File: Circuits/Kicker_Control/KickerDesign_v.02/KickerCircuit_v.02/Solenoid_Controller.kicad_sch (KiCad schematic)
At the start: 8 parts, among them Q2 NMOS, U3 VS-5EWH06FN-M3, U4 VS-5EWH06FN-M3

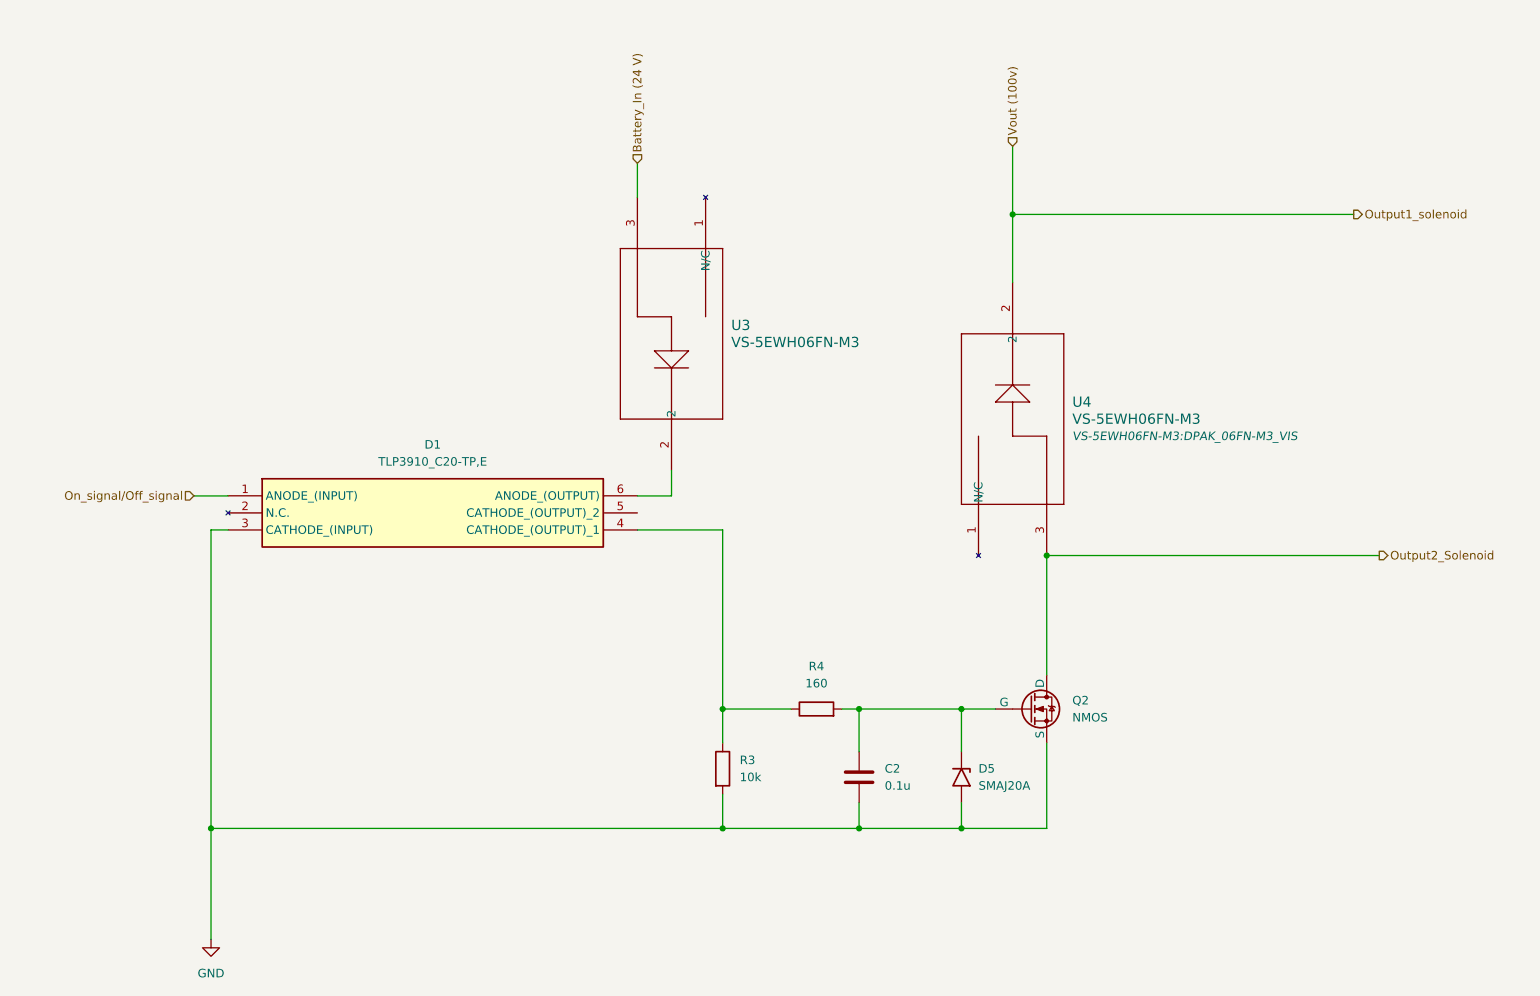
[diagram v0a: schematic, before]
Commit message: Updated the kicker circuit
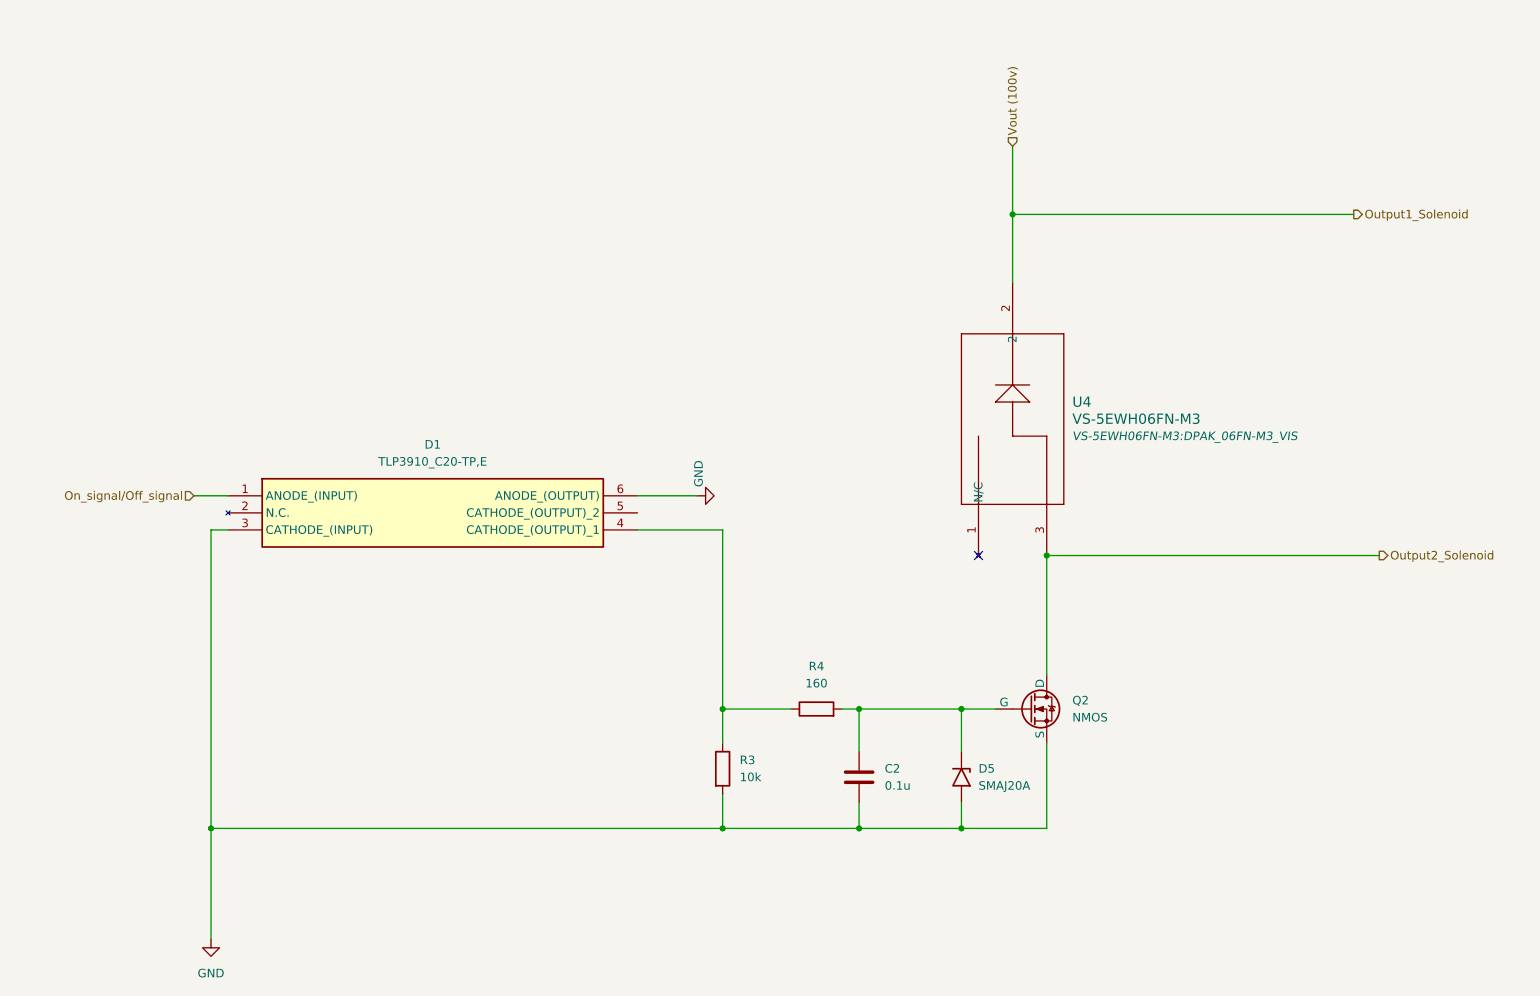
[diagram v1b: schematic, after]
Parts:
- removed U3: VS-5EWH06FN-M3, VS-5EWH06FN-M3:DPAK_06FN-M3_VIS, symbol VS-5EWH06FN-M3:VS-5EWH06FN-M3
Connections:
- net GND: now also D1.6 (ANODE_(OUTPUT))
- net Output1_solenoid renamed Output1_Solenoid
- no-connect marks 0 -> 1

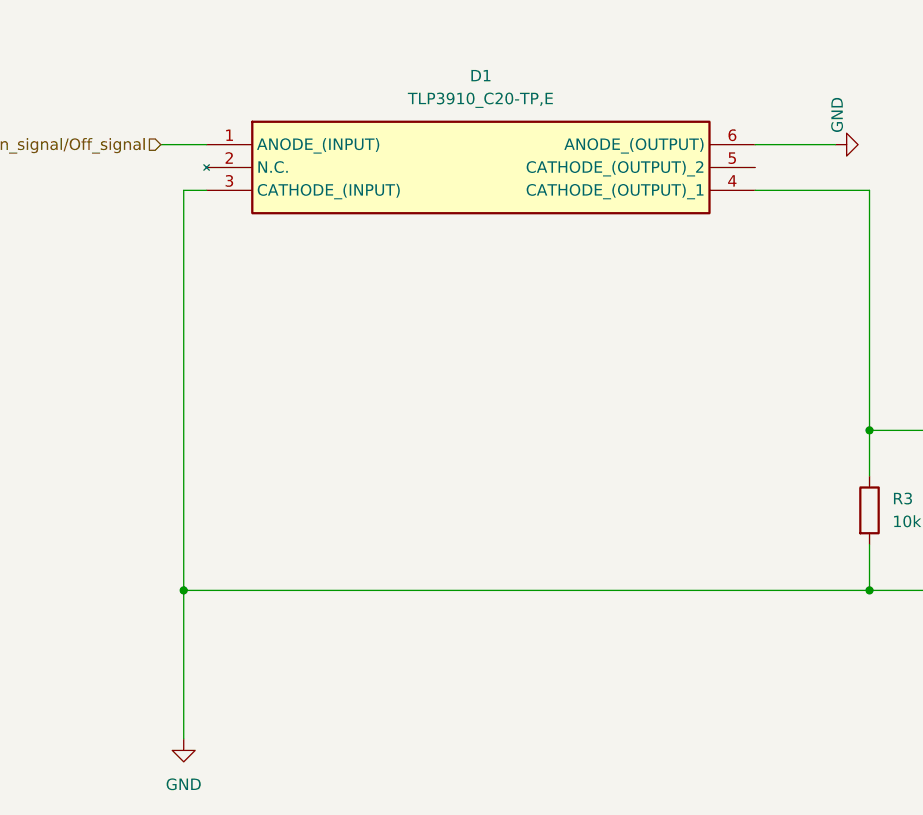
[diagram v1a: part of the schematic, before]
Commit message: updated kicker circuit
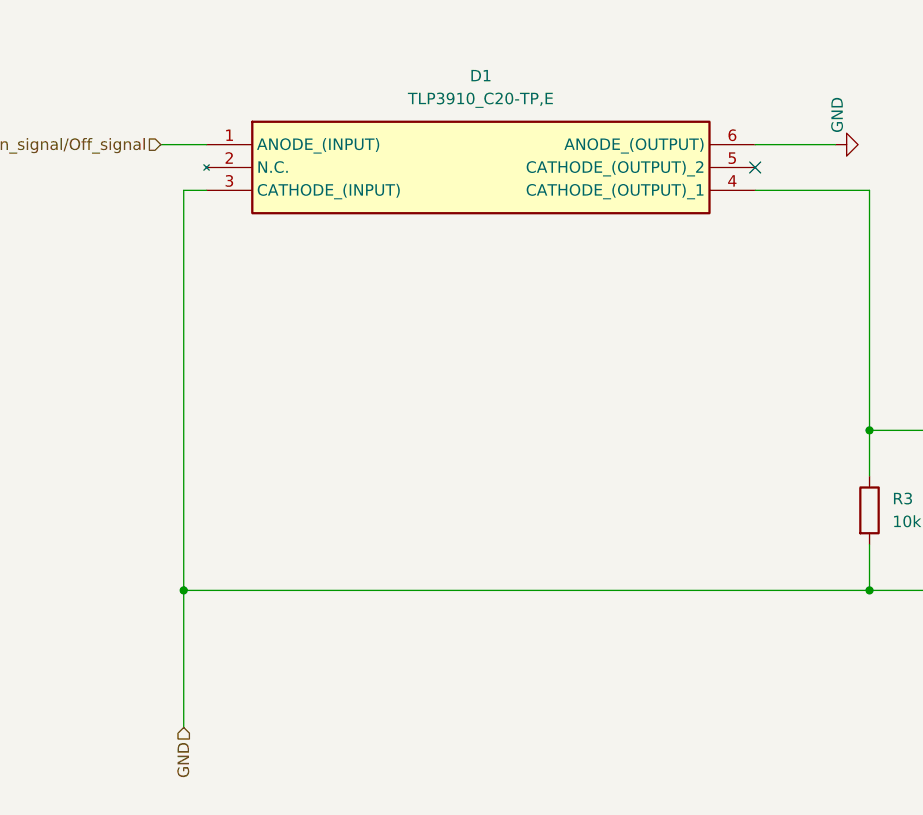
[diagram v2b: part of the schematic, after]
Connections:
- no-connect marks 1 -> 2
